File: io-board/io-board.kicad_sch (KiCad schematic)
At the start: 15 parts, among them J5 Conn_01x24, U1 Littelfuse SP720, U2 Kamod BluePill STM32F103C8T6

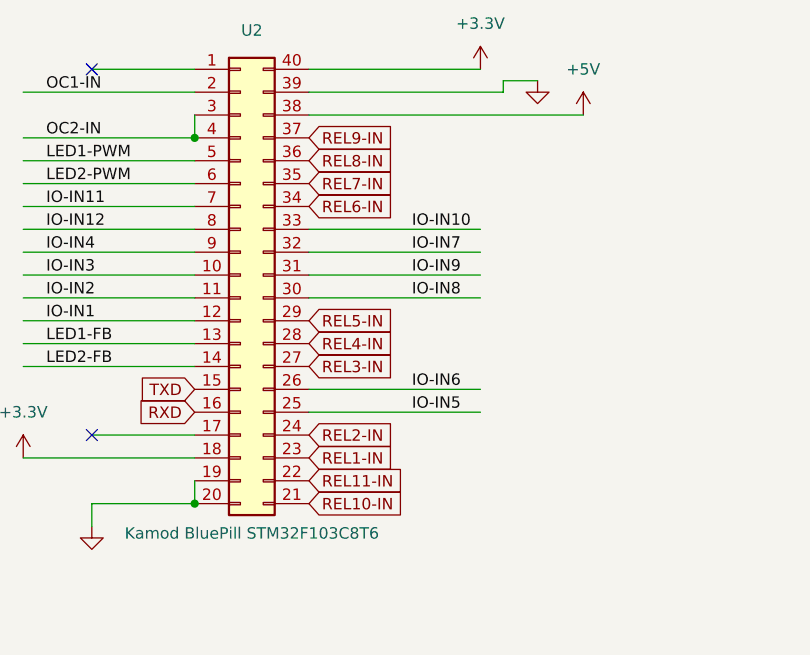
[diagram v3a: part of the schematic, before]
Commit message: PCB: All component locations done
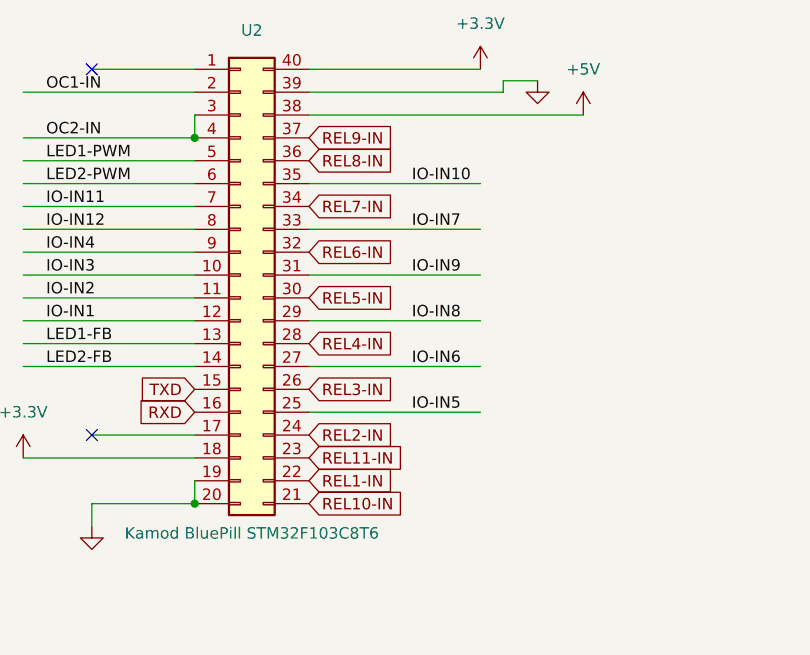
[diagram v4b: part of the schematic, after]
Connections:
- net IO-IN10: now also U2.35 (Pin_35); no longer U2.33 (Pin_33)
- net IO-IN6: now also U2.27 (Pin_27); no longer U2.26 (Pin_26)
- net IO-IN7: now also U2.33 (Pin_33); no longer U2.32 (Pin_32)
- net IO-IN8: now also U2.29 (Pin_29); no longer U2.30 (Pin_30)
- net REL1-IN: now also U2.22 (Pin_22); no longer U2.23 (Pin_23)
- net REL11-IN: now also U2.23 (Pin_23); no longer U2.22 (Pin_22)
- net REL3-IN: now also U2.26 (Pin_26); no longer U2.27 (Pin_27)
- net REL5-IN: now also U2.30 (Pin_30); no longer U2.29 (Pin_29)
- net REL6-IN: now also U2.32 (Pin_32); no longer U2.34 (Pin_34)
- net REL7-IN: now also U2.34 (Pin_34); no longer U2.35 (Pin_35)
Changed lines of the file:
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@@
 	(wire
 		(pts
-			(xy 135.89 46.99) (xy 154.94 46.99)
+			(xy 135.89 49.53) (xy 154.94 49.53)
 		)
 		(stroke
@@
 	(wire
 		(pts
-			(xy 135.89 41.91) (xy 154.94 41.91)
+			(xy 135.89 39.37) (xy 154.94 39.37)
 		)
 		(stroke
@@
 	(wire
 		(pts
-			(xy 135.89 39.37) (xy 154.94 39.37)
+			(xy 135.89 34.29) (xy 154.94 34.29)
 		)
 		(stroke
@@
 	(wire
 		(pts
-			(xy 135.89 57.15) (xy 154.94 57.15)
+			(xy 135.89 54.61) (xy 154.94 54.61)
 		)
 		(stroke
@@
 	)
 	(label "IO-IN6"
-		(at 147.32 57.15 0)
+		(at 147.32 54.61 0)
 		(effects
 			(font
@@
 	)
 	(label "IO-IN7"
-		(at 147.32 41.91 0)
+		(at 147.32 39.37 0)
 		(effects
 			(font
@@
 	)
 	(label "IO-IN10"
-		(at 147.32 39.37 0)
+		(at 147.32 34.29 0)
 		(effects
 			(font
@@
 	)
 	(label "IO-IN8"
-		(at 147.32 46.99 0)
+		(at 147.32 49.53 0)
 		(effects
 			(font
@@
 	(global_label "REL5-IN"
 		(shape input)
-		(at 135.89 49.53 0)
+		(at 135.89 46.99 0)
 		(fields_autoplaced yes)
 		(effects
@@
 		)
 		(property "Intersheetrefs" "${INTERSHEET_REFS}"
-			(at 147.0395 49.53 0)
+			(at 147.0395 46.99 0)
 			(effects
 				(font
@@
 	(global_label "REL3-IN"
 		(shape input)
-		(at 135.89 54.61 0)
+		(at 135.89 57.15 0)
 		(fields_autoplaced yes)
 		(effects
@@
 		)
 		(property "Intersheetrefs" "${INTERSHEET_REFS}"
-			(at 147.0395 54.61 0)
+			(at 147.0395 57.15 0)
 			(effects
 				(font
@@
 	(global_label "REL1-IN"
 		(shape input)
-		(at 135.89 64.77 0)
+		(at 135.89 67.31 0)
 		(fields_autoplaced yes)
 		(effects
@@
 		)
 		(property "Intersheetrefs" "${INTERSHEET_REFS}"
-			(at 147.0395 64.77 0)
+			(at 147.0395 67.31 0)
 			(effects
 				(font
@@
 	(global_label "REL6-IN"
 		(shape input)
+		(at 135.89 41.91 0)
+		(fields_autoplaced yes)
+		(effects
+			(font
+				(size 1.27 1.27)
+			)
+			(justify left)
+		)
+		(property "Intersheetrefs" "${INTERSHEET_REFS}"
+			(at 147.0395 41.91 0)
+			(effects
+				(font
+					(size 1.27 1.27)
+				)
+				(justify left)
+				(hide yes)
+			)
+		)
+	)
+	(global_label "REL7-IN"
+		(shape input)
 		(at 135.89 36.83 0)
 		(fields_autoplaced yes)
@@
 		)
 	)
-	(global_label "REL7-IN"
-		(shape input)
-		(at 135.89 34.29 0)
-		(fields_autoplaced yes)
-		(effects
-			(font
-				(size 1.27 1.27)
-			)
-			(justify left)
-		)
-		(property "Intersheetrefs" "${INTERSHEET_REFS}"
-			(at 147.0395 34.29 0)
-			(effects
-				(font
-					(size 1.27 1.27)
-				)
-				(justify left)
-				(hide yes)
-			)
-		)
-	)
 	(global_label "REL11-OUT2"
 		(shape input)
@@
 	(global_label "REL11-IN"
 		(shape input)
-		(at 135.89 67.31 0)
+		(at 135.89 64.77 0)
 		(fields_autoplaced yes)
 		(effects
@@
 		)
 		(property "Intersheetrefs" "${INTERSHEET_REFS}"
-			(at 148.249 67.31 0)
+			(at 148.249 64.77 0)
 			(effects
 				(font

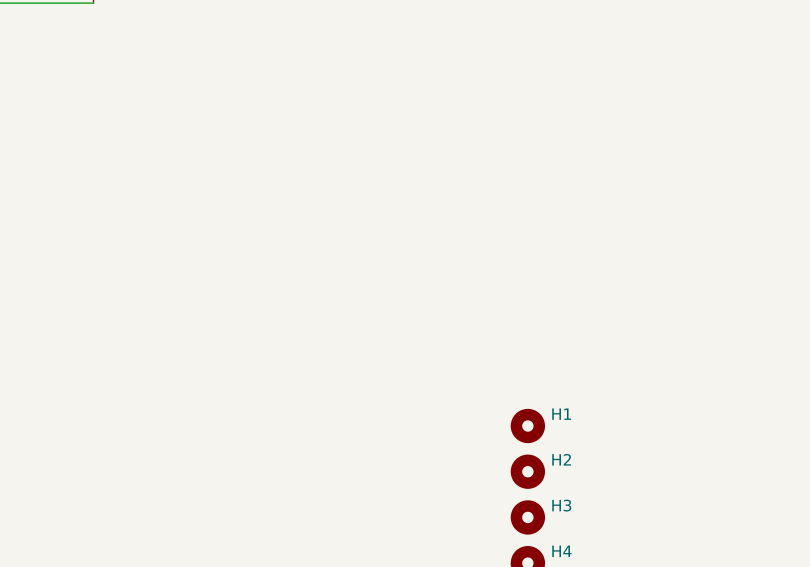
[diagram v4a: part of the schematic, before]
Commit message: PCB: Stencil holders and production configuration
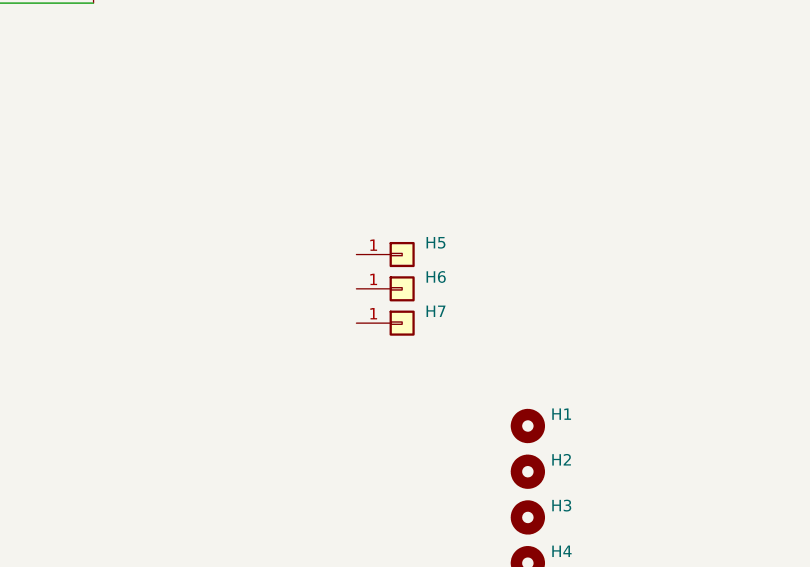
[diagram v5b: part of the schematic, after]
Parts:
- added H5, H6, H7: Conn_01x01, Footprints:stencil-holder, symbol Connector_Generic:Conn_01x01
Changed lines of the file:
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@@
+	)
+	(symbol
+		(lib_id "Connector_Generic:Conn_01x01")
+		(at 200.66 54.61 0)
+		(unit 1)
+		(exclude_from_sim no)
+		(in_bom yes)
+		(on_board yes)
+		(dnp no)
+		(fields_autoplaced yes)
+		(property "Reference" "H5"
+			(at 203.2 53.3399 0)
+			(effects
+				(font
+					(size 1.27 1.27)
+				)
+				(justify left)
+			)
+		)
+		(property "Value" "Conn_01x01"
+			(at 203.2 55.8799 0)
+			(effects
+				(font
+					(size 1.27 1.27)
+				)
+				(justify left)
+				(hide yes)
+			)
+		)
+		(property "Footprint" "Footprints:stencil-holder"
+			(at 200.66 54.61 0)
+			(effects
+				(font
+					(size 1.27 1.27)
+				)
+				(hide yes)
+			)
+		)
+		(property "Datasheet" "~"
+			(at 200.66 54.61 0)
+			(effects
+				(font
+					(size 1.27 1.27)
+				)
+				(hide yes)
+			)
+		)
+		(property "Description" "Generic connector, single row, 01x01, script generated (kicad-library-utils/schlib/autogen/connector/)"
+			(at 200.66 54.61 0)
+			(effects
+				(font
+					(size 1.27 1.27)
+				)
+				(hide yes)
+			)
+		)
+		(pin "1"
+		)
+		(instances
+			(project ""
+				(path "/5a6848ff-426f-432e-bc4d-b6eef5e4348a"
+					(reference "H5")
+					(unit 1)
+				)
+			)
+		)
+	)
+	(symbol
+		(lib_id "Connector_Generic:Conn_01x01")
+		(at 200.66 58.42 0)
+		(unit 1)
+		(exclude_from_sim no)
+		(in_bom yes)
+		(on_board yes)
+		(dnp no)
+		(fields_autoplaced yes)
+		(property "Reference" "H6"
+			(at 203.2 57.1499 0)
+			(effects
+				(font
+					(size 1.27 1.27)
+				)
+				(justify left)
+			)
+		)
+		(property "Value" "Conn_01x01"
+			(at 203.2 59.6899 0)
+			(effects
+				(font
+					(size 1.27 1.27)
+				)
+				(justify left)
+				(hide yes)
+			)
+		)
+		(property "Footprint" "Footprints:stencil-holder"
+			(at 200.66 58.42 0)
+			(effects
+				(font
+					(size 1.27 1.27)
+				)
+				(hide yes)
+			)
+		)
+		(property "Datasheet" "~"
+			(at 200.66 58.42 0)
+			(effects
+				(font
+					(size 1.27 1.27)
+				)
+				(hide yes)
+			)
+		)
+		(property "Description" "Generic connector, single row, 01x01, script generated (kicad-library-utils/schlib/autogen/connector/)"
+			(at 200.66 58.42 0)
+			(effects
+				(font
+					(size 1.27 1.27)
+				)
+				(hide yes)
+			)
+		)
+		(pin "1"
+		)
+		(instances
+			(project "io-board"
+				(path "/5a6848ff-426f-432e-bc4d-b6eef5e4348a"
+					(reference "H6")
+					(unit 1)
+				)
+			)
+		)
 	)
 	(symbol
@@
 					(unit 1)
 				)
+			)
+		)
+	)
+	(symbol
+		(lib_id "Connector_Generic:Conn_01x01")
+		(at 200.66 62.23 0)
+		(unit 1)
+		(exclude_from_sim no)
+		(in_bom yes)
+		(on_board yes)
+		(dnp no)
+		(fields_autoplaced yes)
+		(property "Reference" "H7"
+			(at 203.2 60.9599 0)
+			(effects
+				(font
+					(size 1.27 1.27)
+				)
+				(justify left)
+			)
+		)
+		(property "Value" "Conn_01x01"
+			(at 203.2 63.4999 0)
+			(effects
+				(font
+					(size 1.27 1.27)
+				)
+				(justify left)
+				(hide yes)
+			)
+		)
+		(property "Footprint" "Footprints:stencil-holder"
+			(at 200.66 62.23 0)
+			(effects
+				(font
+					(size 1.27 1.27)
+				)
+				(hide yes)
+			)
+		)
+		(property "Datasheet" "~"
+			(at 200.66 62.23 0)
+			(effects
+				(font
+					(size 1.27 1.27)
+				)
+				(hide yes)
+			)
+		)
+		(property "Description" "Generic connector, single row, 01x01, script generated (kicad-library-utils/schlib/autogen/connector/)"
+			(at 200.66 62.23 0)
+			(effects
+				(font
+					(size 1.27 1.27)
+				)
+				(hide yes)
+			)
+		)
+		(pin "1"
+		)
+		(instances
+			(project "io-board"
+				(path "/5a6848ff-426f-432e-bc4d-b6eef5e4348a"
+					(reference "H7")
+					(unit 1)
+				)

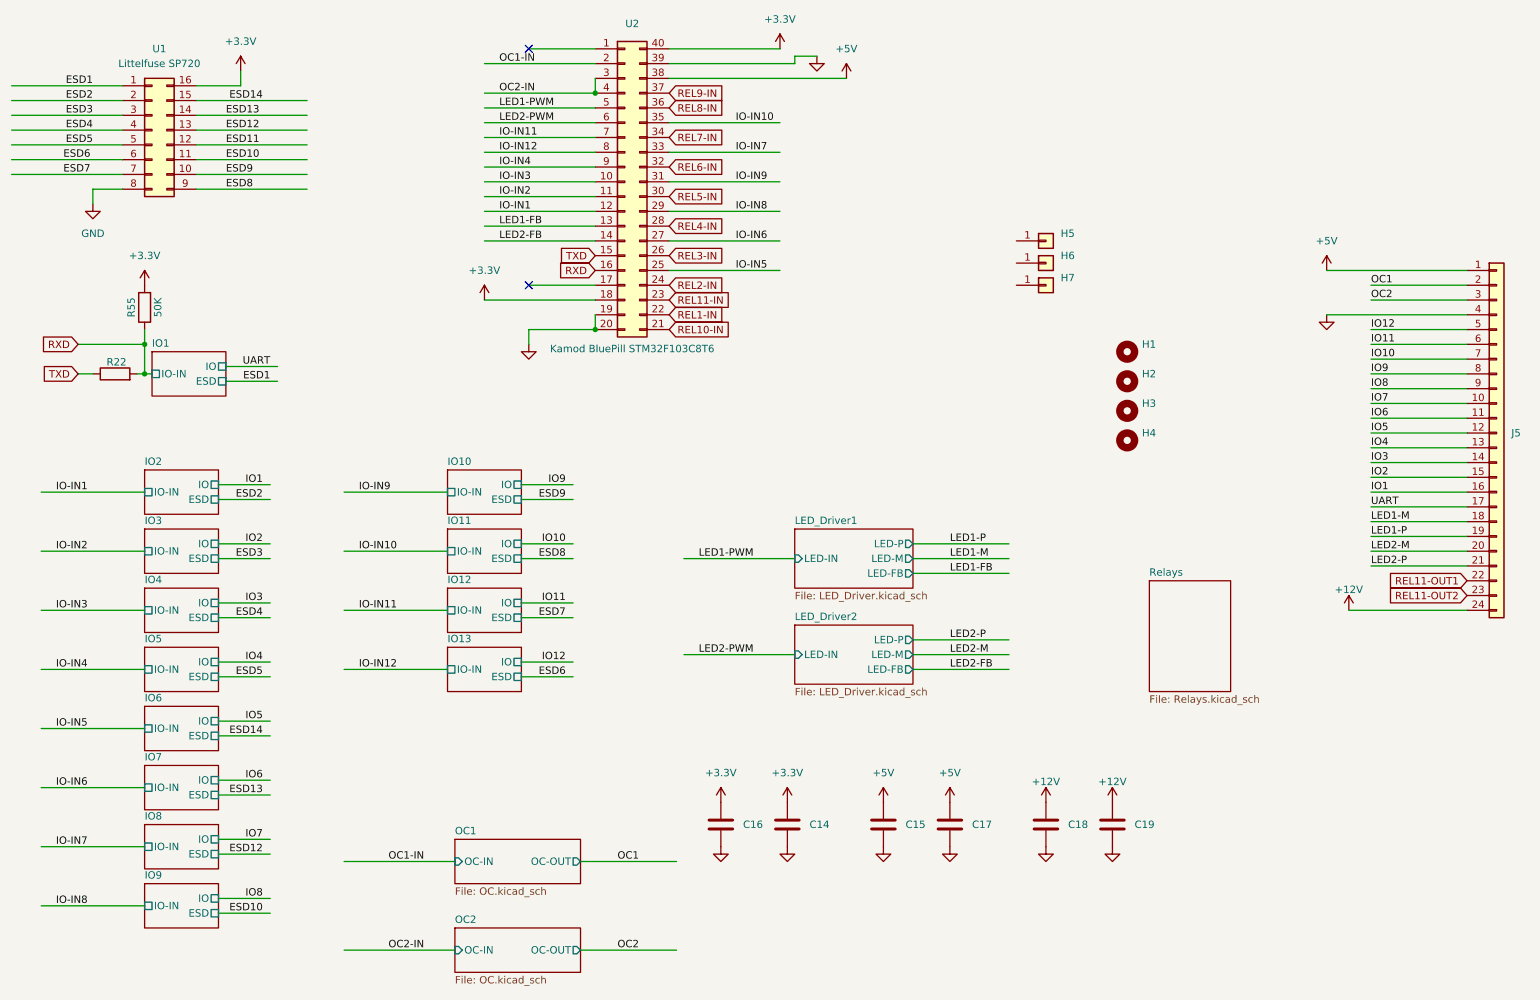
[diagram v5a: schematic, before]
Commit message: PCB: io-board: component values and BOM
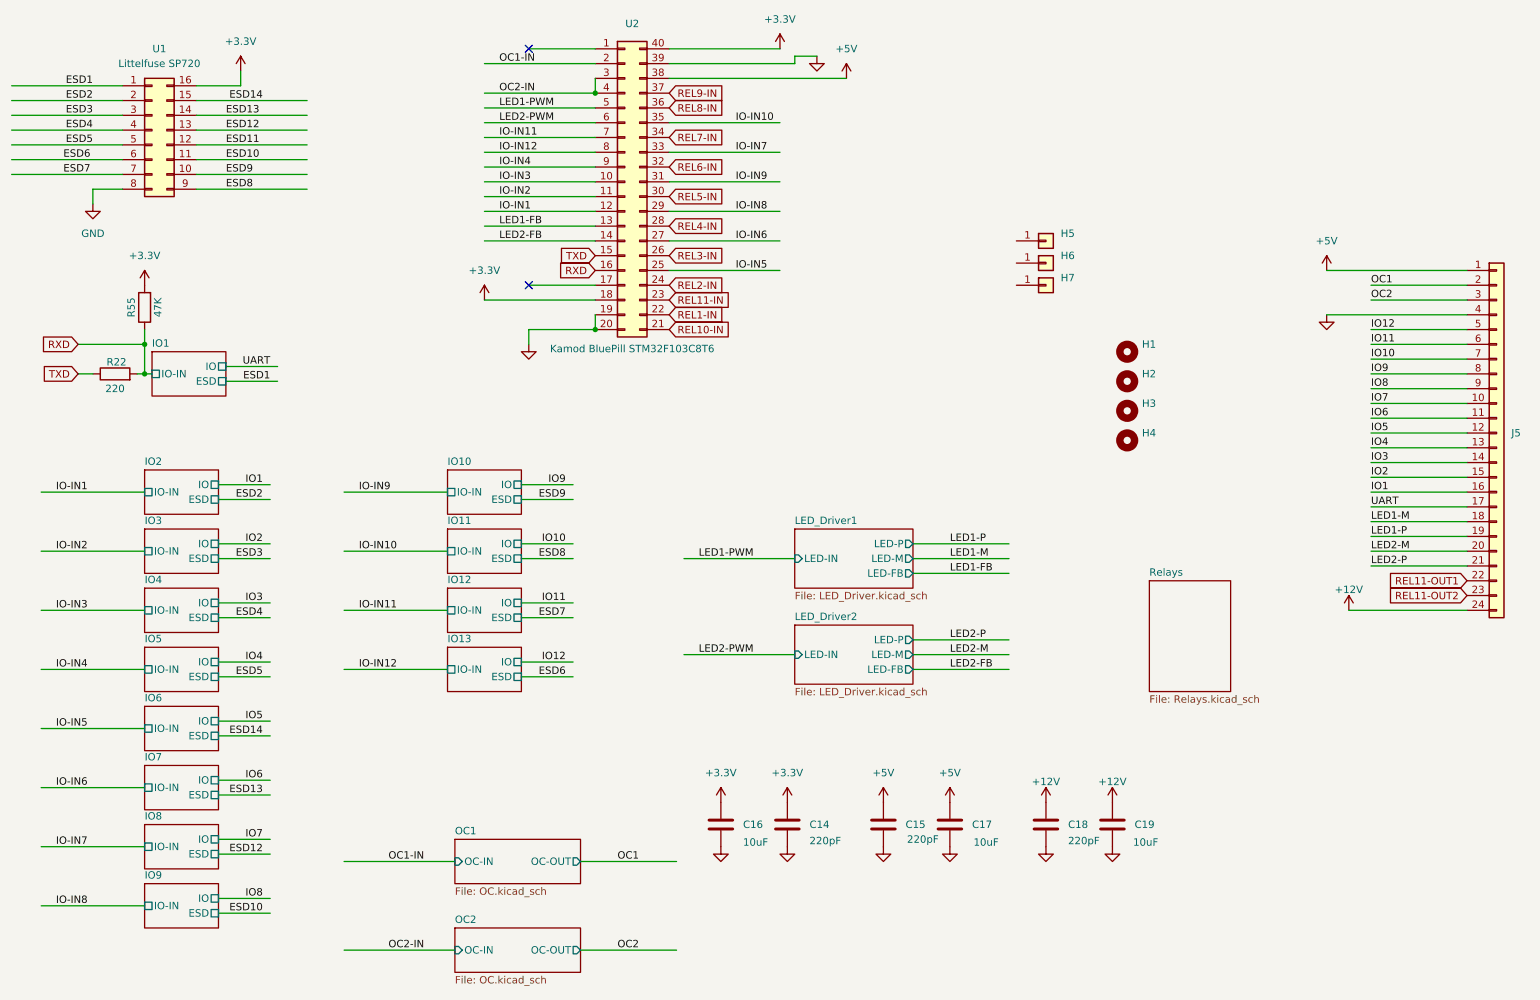
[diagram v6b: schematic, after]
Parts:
- C14, C15, C18: value C -> 220pF
- C16, C17, C19: value C -> 10uF
- R22: value R -> 220
- R55: value 50K -> 47K
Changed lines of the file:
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@@
 		(on_board yes)
 		(dnp no)
-		(fields_autoplaced yes)
 		(property "Reference" "C16"
 			(at 148.59 154.9399 0)
@@
 			)
 		)
-		(property "Value" "C"
-			(at 148.59 156.2099 0)
-			(effects
-				(font
-					(size 1.27 1.27)
-				)
-				(justify left)
-				(hide yes)
+		(property "Value" "10uF"
+			(at 148.59 157.988 0)
+			(effects
+				(font
+					(size 1.27 1.27)
+				)
+				(justify left)
 			)
 		)
@@
 		(on_board yes)
 		(dnp no)
-		(fields_autoplaced yes)
 		(property "Reference" "C15"
 			(at 176.53 154.9399 0)
@@
 			)
 		)
-		(property "Value" "C"
-			(at 176.53 156.2099 0)
-			(effects
-				(font
-					(size 1.27 1.27)
-				)
-				(justify left)
-				(hide yes)
+		(property "Value" "220pF"
+			(at 176.784 157.48 0)
+			(effects
+				(font
+					(size 1.27 1.27)
+				)
+				(justify left)
 			)
 		)
@@
 			)
 		)
-		(property "Value" "R"
-			(at 38.862 75.438 90)
-			(effects
-				(font
-					(size 1.27 1.27)
-				)
-				(hide yes)
+		(property "Value" "220"
+			(at 40.64 80.01 90)
+			(effects
+				(font
+					(size 1.27 1.27)
+				)
 			)
 		)
@@
 		(on_board yes)
 		(dnp no)
-		(fields_autoplaced yes)
 		(property "Reference" "C18"
 			(at 204.47 154.9399 0)
@@
 			)
 		)
-		(property "Value" "C"
-			(at 204.47 156.2099 0)
-			(effects
-				(font
-					(size 1.27 1.27)
-				)
-				(justify left)
-				(hide yes)
+		(property "Value" "220pF"
+			(at 204.47 157.734 0)
+			(effects
+				(font
+					(size 1.27 1.27)
+				)
+				(justify left)
 			)
 		)
@@
 		(on_board yes)
 		(dnp no)
-		(fields_autoplaced yes)
 		(property "Reference" "C17"
 			(at 187.96 154.9399 0)
@@
 			)
 		)
-		(property "Value" "C"
-			(at 187.96 156.2099 0)
-			(effects
-				(font
-					(size 1.27 1.27)
-				)
-				(justify left)
-				(hide yes)
+		(property "Value" "10uF"
+			(at 188.214 157.988 0)
+			(effects
+				(font
+					(size 1.27 1.27)
+				)
+				(justify left)
 			)
 		)
@@
 			)
 		)
-		(property "Value" "50K"
+		(property "Value" "47K"
 			(at 48.006 66.04 90)
 			(effects
@@
 		(on_board yes)
 		(dnp no)
-		(fields_autoplaced yes)
 		(property "Reference" "C14"
 			(at 160.02 154.9399 0)
@@
 			)
 		)
-		(property "Value" "C"
-			(at 160.02 156.2099 0)
-			(effects
-				(font
-					(size 1.27 1.27)
-				)
-				(justify left)
-				(hide yes)
+		(property "Value" "220pF"
+			(at 160.02 157.734 0)
+			(effects
+				(font
+					(size 1.27 1.27)
+				)
+				(justify left)
 			)
 		)
@@
 		(on_board yes)
 		(dnp no)
-		(fields_autoplaced yes)
 		(property "Reference" "C19"
 			(at 215.9 154.9399 0)
@@
 			)
 		)
-		(property "Value" "C"
-			(at 215.9 156.2099 0)
-			(effects
-				(font
-					(size 1.27 1.27)
-				)
-				(justify left)
-				(hide yes)
-			)
-		)
+		(property "Value" "10uF"
+			(at 215.646 157.988 0)
+			(effects
+				(font
+					(size 1.27 1.27)
+				)
+				(justify left)
+			)
+		)
